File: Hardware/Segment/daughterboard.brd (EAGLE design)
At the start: 210.8 x 51.8 mm, 163 parts, among them IC1 PBQ79656PAPTQ1, IC2 PBQ79656PAPTQ1, T1 PBHV8115X, 115, T2 PBHV8115X, 115

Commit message: Dummy battery and daughterboard v1.1
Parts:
- added DISABLE_UART: Disable UART, jumper:SJ
- added GND, RX, TX: (no value), wirepad:2,54/1,0
- added GNDH, GNDL: (no value), wirepad:SMD2,54-5,08
- added NFAULT: TPB2,54, testpad:B2,54
- moved CTSREF1 25.4 mm to (64.8, 39.4)
- moved TEMPR6 25.4 mm to (52.7, 39.4)
- moved SR 25.4 mm to (20.3, 45.7)
- moved TEMPL 25.4 mm to (48.3, 45.7)
- moved TEMPR1 25.4 mm to (31.8, 39.4)
- moved TEMPR2 25.4 mm to (35.6, 39.4)
- moved TEMPR3 25.4 mm to (40.0, 39.4)
- moved TEMPR5 25.4 mm to (48.9, 39.4)
- moved TEMPR7 25.4 mm to (57.1, 39.4)
- moved TEMPR8 25.4 mm to (61.0, 39.4)
- moved TEMPR4 25.4 mm to (44.5, 39.4)
- moved CCVDD 1.27 mm to (86.4, 29.2)
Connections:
- new net N$10: IC1.62, NFAULT.TP
- new net N$3: DISABLE_UART.2, IC1.52, RX.1
- new net N$9: IC1.53, TX.1
- net CVDD: now also DISABLE_UART.1; no longer IC1.52
- net GNDH: now also GNDH.1
- net GNDL: now also GND.1, GNDL.1
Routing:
- net N$7: track 34.5 -> 60.7 mm
- net N$4: track 30.9 -> 56.3 mm
- net N$3: track 0.00 -> 24.7 mm
- net TSREF: track 42.4 -> 64.9 mm
- net TEMP1: track 40.0 -> 58.2 mm
- net TEMP2: track 37.1 -> 54.8 mm
- net TEMP3: track 34.7 -> 51.8 mm
- net TEMP4: track 31.6 -> 48.6 mm
- net TEMP5: track 28.8 -> 45.1 mm
- net TEMP6: track 29.6 -> 43.7 mm
- net N$9: track 0.00 -> 13.4 mm
- net TEMP7: track 32.5 -> 41.3 mm
- net N$10: track 0.00 -> 4.83 mm
- net TEMP8: track 36.4 -> 37.6 mm
- net NPNB: track 19.1 -> 18.3 mm
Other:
- board text added: "BMS Daughterboard V1.1 Joshua Feist January 2022"
- board text added: "Cell Balancing"
- board text added: "Shunt Resistor (Current Sense)"
- board text added: "Thermistors"
- board text added: "Voltage Sense"
- board text removed: "BMS Daughterboard V1 Joshua Feist"

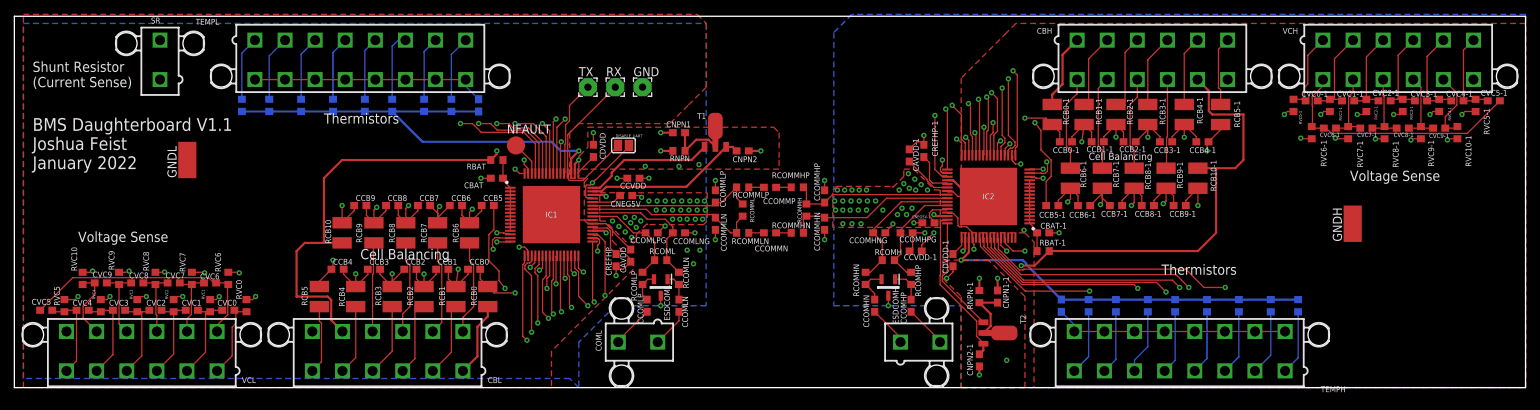
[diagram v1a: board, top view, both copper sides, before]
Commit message: Rotated connector to shrink board
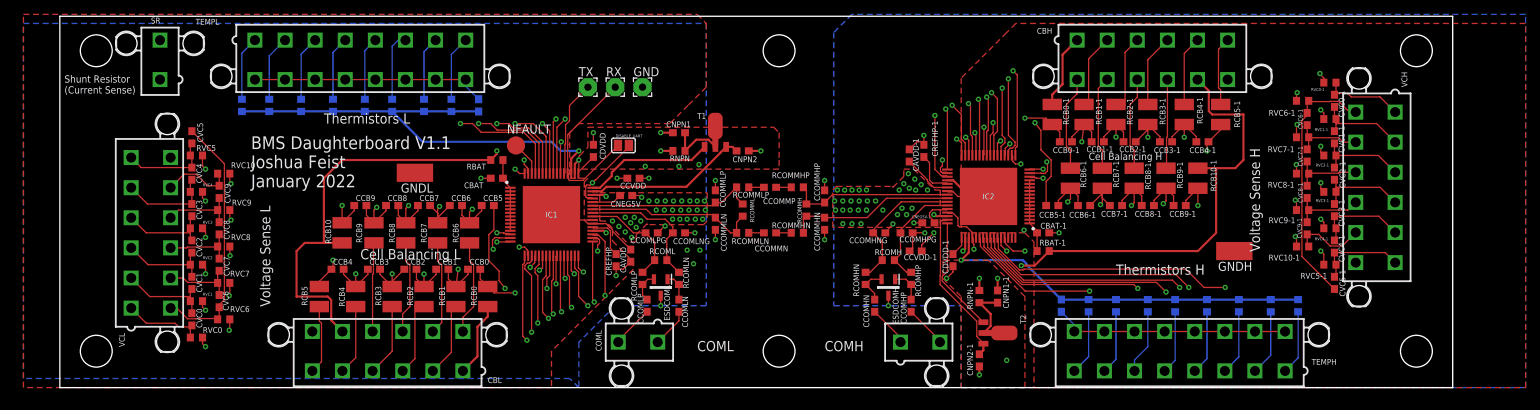
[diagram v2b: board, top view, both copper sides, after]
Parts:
- moved CVC5-1 33.8 mm to (184.2, 14.6), turned to 90 degrees
- moved GNDL 31.8 mm to (55.9, 30.0), turned to 90 degrees
- moved CVC5 31.5 mm to (24.8, 34.9), turned to 270 degrees
- moved RVC5-1 30.1 mm to (183.5, 17.1), turned to 180 degrees
- moved RVC5 27.9 mm to (25.4, 32.4), turned to 0 degrees
- moved RVC10-1 26.8 mm to (179.7, 19.7), turned to 180 degrees
- moved CVC4-1 26.6 mm to (184.2, 19.7), turned to 90 degrees
- moved RVC10 24.5 mm to (29.2, 29.8), turned to 0 degrees
- moved CVC4 24.4 mm to (24.8, 29.8), turned to 270 degrees
- moved CVC9-1 23.1 mm to (180.3, 22.2), turned to 90 degrees
- moved RVC4-1 22.9 mm to (183.5, 22.2), turned to 180 degrees
- moved CVC9 20.8 mm to (28.6, 27.3), turned to 270 degrees
- moved RVC4 20.7 mm to (25.4, 27.3), turned to 0 degrees
- moved RVC9-1 19.7 mm to (179.7, 24.8), turned to 180 degrees
- moved CVC3-1 19.4 mm to (184.2, 24.8), turned to 90 degrees
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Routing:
- net VC9: track 94.5 -> 114.3 mm
- net VC9-1: track 94.5 -> 113.5 mm
- net VC8: track 97.7 -> 116.6 mm
- net VC7: track 106.6 -> 125.0 mm
- net VC6: track 108.8 -> 126.6 mm
- net VC8-1: track 97.7 -> 114.2 mm
- net VC7-1: track 106.6 -> 122.5 mm
- net VC10-1: track 62.6 -> 48.0 mm
- net VC6-1: track 108.8 -> 123.4 mm
- net VC5: track 77.7 -> 91.8 mm
- net VC5-1: track 77.7 -> 91.7 mm
- net VC4-1: track 73.2 -> 86.5 mm
- net VC4: track 73.2 -> 86.5 mm
- net VC10: track 62.6 -> 49.8 mm
- net VC3-1: track 68.8 -> 81.5 mm
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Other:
- board size 210.8 x 51.8 mm -> 194.3 x 51.8 mm
- board text added: "COMH"
- board text added: "COML"
- board text added: "Cell Balancing H"
- board text added: "Cell Balancing L"
- board text added: "Thermistors H"
- board text added: "Thermistors L"
- board text added: "Voltage Sense H"
- board text added: "Voltage Sense L"
- board text removed: "Cell Balancing"
- board text removed: "Thermistors"
- board text removed: "Voltage Sense"

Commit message: Mainboard routing
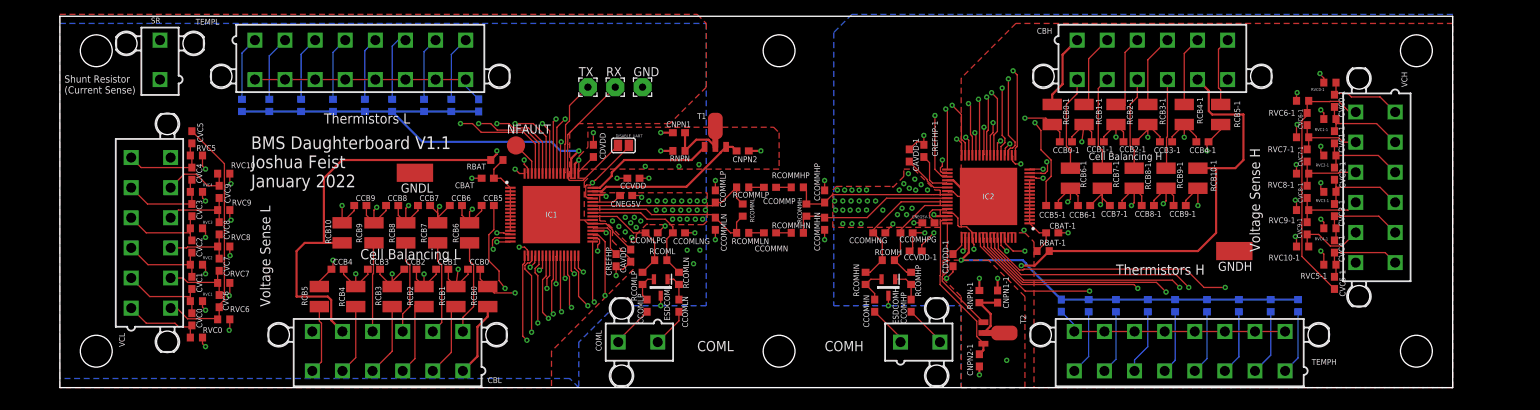
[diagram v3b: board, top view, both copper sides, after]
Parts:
- moved CBAT-1 1.27 mm to (144.8, 21.6)
- moved CBAT 1.27 mm to (66.0, 29.2)
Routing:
- net VC_CB_HIGH-1: track 10.3 -> 11.9 mm
- net VC_CB_HIGH: track 10.3 -> 11.9 mm
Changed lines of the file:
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@@
 </layers>
 <board>
-<fusionsync huburn="a.cGVyc29uYWw6dWUyYmIzODJk" projecturn="a.cGVyc29uYWw6dWUyYmIzODJkIzIwMjEwNTAxNDA4NDA5OTU2" f3durn="urn:adsk.wipprod:dm.lineage:KUb0E9VYR3-2wecNlMESeA" pcbguid="" lastpulledtime="" lastsyncedchangeguid="" latestrevisionid="15230511-20a2-40cb-83f5-cf13ab4d5c8c" lastsyncedrevisionid="15230511-20a2-40cb-83f5-cf13ab4d5c8c" lastboardhashguid="42d6915e-be4c-94d1-d2e9-ec4e673c003c" lastpushedtime="2022-01-14T15:47:41Z" linktopcb3d="true"/>
+<fusionsync huburn="a.cGVyc29uYWw6dWUyYmIzODJk" projecturn="a.cGVyc29uYWw6dWUyYmIzODJkIzIwMjEwNTAxNDA4NDA5OTU2" f3durn="urn:adsk.wipprod:dm.lineage:KUb0E9VYR3-2wecNlMESeA" pcbguid="" lastpulledtime="" lastsyncedchangeguid="" latestrevisionid="15230511-20a2-40cb-83f5-cf13ab4d5c8c" lastsyncedrevisionid="15230511-20a2-40cb-83f5-cf13ab4d5c8c" lastboardhashguid="42d6915e-be4c-94d1-d2e9-ec4e673c003c" lastpushedtime="2022-01-14T15:47:41Z" linktopcb3d="false"/>
 <plain>
 <wire x1="6.35" y1="0" x2="200.64" y2="0" width="0" layer="20"/>
@@
 <attribute name="VALUE" x="59.055" y="14.605" size="0.6096" layer="27"/>
 </element>
-<element name="CBAT" library="rcl" library_urn="urn:adsk.eagle:library:334" package="C0603" package3d_urn="urn:adsk.eagle:package:23616/2" value="10 nf" x="67.31" y="29.21" smashed="yes">
-<attribute name="NAME" x="62.738" y="27.813" size="0.8128" layer="25"/>
-<attribute name="POPULARITY" value="73" x="152.4" y="-16.51" size="1.778" layer="27" display="off"/>
-<attribute name="SPICEPREFIX" value="C" x="152.4" y="-16.51" size="1.778" layer="27" display="off"/>
-<attribute name="VALUE" x="67.945" y="27.305" size="0.6096" layer="27"/>
+<element name="CBAT" library="rcl" library_urn="urn:adsk.eagle:library:334" package="C0603" package3d_urn="urn:adsk.eagle:package:23616/2" value="10 nf" x="66.04" y="29.21" smashed="yes">
+<attribute name="NAME" x="61.468" y="27.813" size="0.8128" layer="25"/>
+<attribute name="POPULARITY" value="73" x="151.13" y="-16.51" size="1.778" layer="27" display="off"/>
+<attribute name="SPICEPREFIX" value="C" x="151.13" y="-16.51" size="1.778" layer="27" display="off"/>
+<attribute name="VALUE" x="66.675" y="27.305" size="0.6096" layer="27"/>
 </element>
 <element name="CREFHP" library="rcl" library_urn="urn:adsk.eagle:library:334" package="C0603" package3d_urn="urn:adsk.eagle:package:23616/2" value="1uf" x="83.947" y="17.78" smashed="yes" rot="R90">
@@
 <attribute name="VALUE" x="152.4" y="35.687" size="0.6096" layer="27" rot="R180"/>
 </element>
-<element name="CBAT-1" library="rcl" library_urn="urn:adsk.eagle:library:334" package="C0603" package3d_urn="urn:adsk.eagle:package:23616/2" value="10 nf" x="143.51" y="21.59" smashed="yes" rot="R180">
-<attribute name="NAME" x="146.812" y="22.987" size="0.8128" layer="25" rot="R180"/>
-<attribute name="POPULARITY" value="73" x="58.42" y="67.31" size="1.778" layer="27" rot="R180" display="off"/>
-<attribute name="SPICEPREFIX" value="C" x="58.42" y="67.31" size="1.778" layer="27" rot="R180" display="off"/>
-<attribute name="VALUE" x="144.399" y="21.336" size="0.6096" layer="27" rot="R180"/>
+<element name="CBAT-1" library="rcl" library_urn="urn:adsk.eagle:library:334" package="C0603" package3d_urn="urn:adsk.eagle:package:23616/2" value="10 nf" x="144.78" y="21.59" smashed="yes" rot="R180">
+<attribute name="NAME" x="148.082" y="22.987" size="0.8128" layer="25" rot="R180"/>
+<attribute name="POPULARITY" value="73" x="59.69" y="67.31" size="1.778" layer="27" rot="R180" display="off"/>
+<attribute name="SPICEPREFIX" value="C" x="59.69" y="67.31" size="1.778" layer="27" rot="R180" display="off"/>
+<attribute name="VALUE" x="145.669" y="21.336" size="0.6096" layer="27" rot="R180"/>
 </element>
 <element name="CREFHP-1" library="rcl" library_urn="urn:adsk.eagle:library:334" package="C0603" package3d_urn="urn:adsk.eagle:package:23616/2" value="1uf" x="126.873" y="33.02" smashed="yes" rot="R270">
@@
 <wire x1="69.192" y1="26.88" x2="69.192" y2="27.38" width="0.1524" layer="1"/>
 <wire x1="69.192" y1="27.38" x2="69.192" y2="27.88" width="0.1524" layer="1"/>
-<wire x1="69.192" y1="27.88" x2="68.16" y2="28.912" width="0.1524" layer="1"/>
-<wire x1="68.16" y1="28.912" x2="68.16" y2="29.21" width="0.1524" layer="1"/>
-<wire x1="68.16" y1="29.21" x2="68.16" y2="31.75" width="0.1524" layer="1"/>
+<wire x1="69.192" y1="27.88" x2="67.862" y2="29.21" width="0.1524" layer="1"/>
+<wire x1="67.862" y1="29.21" x2="66.89" y2="29.21" width="0.1524" layer="1"/>
+<wire x1="66.89" y1="30.48" x2="68.16" y2="31.75" width="0.1524" layer="1"/>
+<wire x1="66.89" y1="30.48" x2="66.89" y2="29.21" width="0.1524" layer="1"/>
 </signal>
 <signal name="N$33">
@@
 <wire x1="64.77" y1="40.22" x2="62.96" y2="42.03" width="0.1524" layer="16"/>
 <wire x1="62.96" y1="42.03" x2="62.96" y2="42.97" width="0.1524" layer="16"/>
-<wire x1="66.46" y1="29.21" x2="65.0875" y2="29.21" width="0.1524" layer="1"/>
-<via x="65.0875" y="29.21" extent="1-16" drill="0.35"/>
+<wire x1="65.19" y1="29.21" x2="63.8175" y2="29.21" width="0.1524" layer="1"/>
+<via x="63.8175" y="29.21" extent="1-16" drill="0.35"/>
 <polygon width="0.1524" layer="1">
 <vertex x="80.01" y="30.48"/>
@@
 <vertex x="86.36" y="17.78"/>
 <vertex x="86.36" y="16.51"/>
-<vertex x="82.55" y="12.7"/>
 <vertex x="74.93" y="5.08"/>
 <vertex x="74.93" y="0"/>
-<vertex x="1.27" y="0"/>
-<vertex x="1.27" y="52.07"/>
+<vertex x="6.35" y="0"/>
+<vertex x="6.35" y="52.07"/>
 <vertex x="95.25" y="52.07"/>
 <vertex x="96.52" y="50.8"/>
 <vertex x="96.52" y="41.91"/>
-<vertex x="93.98" y="39.37"/>
 <vertex x="91.44" y="36.83"/>
 <vertex x="78.74" y="36.83"/>
 <vertex x="77.47" y="35.56"/>
-<vertex x="77.47" y="30.48"/>
 <vertex x="77.47" y="29.21"/>
 <vertex x="80.01" y="29.21"/>
 <vertex x="79.502" y="28.702"/>
-<vertex x="79.502" y="27.559"/>
 <vertex x="79.502" y="23.368"/>
 <vertex x="80.01" y="22.86"/>
@@
 </polygon>
 <polygon width="0.1524" layer="16">
-<vertex x="1.27" y="50.8"/>
+<vertex x="6.35" y="50.8"/>
 <vertex x="96.52" y="50.8"/>
 <vertex x="96.52" y="11.43"/>
@@
 <vertex x="78.74" y="0"/>
 <vertex x="77.47" y="1.27"/>
-<vertex x="1.27" y="1.27"/>
+<vertex x="6.35" y="1.27"/>
 </polygon>
 <polygon width="0.1524" layer="2">
@@
 <wire x1="146.05" y1="10.58" x2="147.86" y2="8.77" width="0.1524" layer="16"/>
 <wire x1="147.86" y1="8.77" x2="147.86" y2="7.83" width="0.1524" layer="16"/>
-<wire x1="144.36" y1="21.59" x2="145.7325" y2="21.59" width="0.1524" layer="1"/>
-<via x="145.7325" y="21.59" extent="1-16" drill="0.35"/>
+<wire x1="145.63" y1="21.59" x2="147.0025" y2="21.59" width="0.1524" layer="1"/>
+<via x="147.0025" y="21.59" extent="1-16" drill="0.35"/>
 <contactref element="CNPN2-1" pad="1"/>
 <wire x1="134.62" y1="2.96" x2="134.62" y2="1.778" width="0.3048" layer="1"/>
@@
 <polygon width="0.1524" layer="1">
 <vertex x="142.24" y="0"/>
-<vertex x="210.82" y="0"/>
-<vertex x="210.82" y="50.8"/>
+<vertex x="200.66" y="0"/>
+<vertex x="200.66" y="50.8"/>
 <vertex x="139.7" y="50.8"/>
-<vertex x="138.43" y="49.53"/>
 <vertex x="132.08" y="43.18"/>
 <vertex x="132.08" y="21.59"/>
@@
 <polygon width="0.1524" layer="2">
 <vertex x="142.24" y="0"/>
-<vertex x="210.82" y="0"/>
-<vertex x="210.82" y="50.8"/>
+<vertex x="200.66" y="0"/>
+<vertex x="200.66" y="50.8"/>
 <vertex x="139.7" y="50.8"/>
-<vertex x="138.43" y="49.53"/>
 <vertex x="132.08" y="43.18"/>
 <vertex x="132.08" y="21.59"/>
@@
 <polygon width="0.1524" layer="16">
 <vertex x="132.08" y="0"/>
-<vertex x="210.82" y="0"/>
-<vertex x="210.82" y="52.07"/>
+<vertex x="200.66" y="0"/>
+<vertex x="200.66" y="52.07"/>
 <vertex x="116.84" y="52.07"/>
 <vertex x="114.3" y="49.53"/>
@@
 <wire x1="141.628" y1="23.92" x2="141.628" y2="23.42" width="0.1524" layer="1"/>
 <wire x1="141.628" y1="23.42" x2="141.628" y2="22.92" width="0.1524" layer="1"/>
-<wire x1="141.628" y1="22.92" x2="142.66" y2="21.888" width="0.1524" layer="1"/>
-<wire x1="142.66" y1="21.888" x2="142.66" y2="21.59" width="0.1524" layer="1"/>
-<wire x1="142.66" y1="21.59" x2="142.66" y2="19.05" width="0.1524" layer="1"/>
+<wire x1="141.628" y1="22.92" x2="142.958" y2="21.59" width="0.1524" layer="1"/>
+<wire x1="142.958" y1="21.59" x2="143.93" y2="21.59" width="0.1524" layer="1"/>
+<wire x1="143.93" y1="21.59" x2="143.93" y2="20.32" width="0.1524" layer="1"/>
+<wire x1="143.93" y1="20.32" x2="142.66" y2="19.05" width="0.1524" layer="1"/>
 </signal>
 <signal name="N$111">

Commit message: All components on top of daughterboard
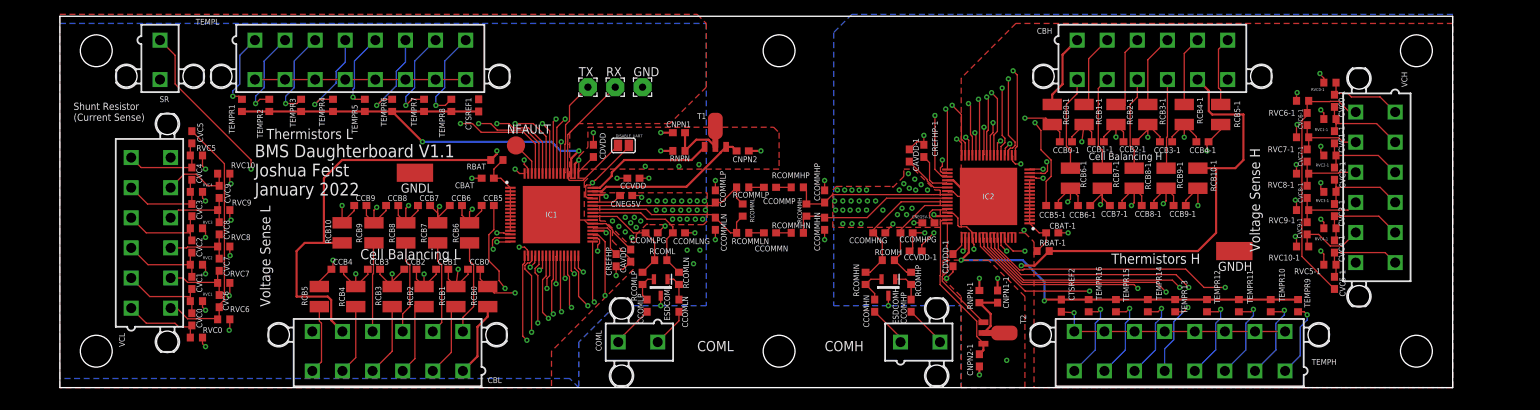
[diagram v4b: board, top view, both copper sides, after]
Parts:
- CCOMHNG, CCOMHPG, CCOMLNG, CCOMLPG: value 220 pF -> 220pf
- CTSREF1, CTSREF2: value 1 uF -> 1uf
- flipped CTSREF1 to the top
- flipped CTSREF2 to the top
- turned SR to 180 degrees
- flipped TEMPR1 to the top
- flipped TEMPR10 to the top
- flipped TEMPR11 to the top
- flipped TEMPR12 to the top
- flipped TEMPR13 to the top
- flipped TEMPR14 to the top
- flipped TEMPR15 to the top
- flipped TEMPR16 to the top
- flipped TEMPR2 to the top
- flipped TEMPR3 to the top
- flipped TEMPR4 to the top
- flipped TEMPR5 to the top
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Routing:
- net N$4: track 56.3 -> 61.7 mm, vias 1 -> 2
- net TEMP7: track 41.3 -> 46.1 mm, vias 1 -> 2
- net TEMP4: track 48.6 -> 53.2 mm, vias 1 -> 2
- net TEMP8: track 37.6 -> 41.9 mm, vias 1 -> 2
- net TEMP12: track 52.2 -> 56.2 mm, vias 1 -> 2
- net TEMP3: track 51.8 -> 55.7 mm, vias 1 -> 2
- net TEMP6: track 43.7 -> 47.3 mm, vias 1 -> 2
- net TEMP2: track 54.8 -> 58.3 mm, vias 1 -> 2
- net GNDL: track 75.3 -> 71.8 mm
- net TEMP11: track 58.4 -> 61.8 mm, vias 1 -> 2
- net TEMP15: track 47.6 -> 50.9 mm, vias 1 -> 2
- net TEMP14: track 50.7 -> 54.1 mm, vias 1 -> 2
- net TEMP13: track 51.4 -> 54.8 mm, vias 1 -> 2
- net N$7: track 60.7 -> 57.6 mm
- net TEMP10: track 62.9 -> 65.9 mm, vias 1 -> 2
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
